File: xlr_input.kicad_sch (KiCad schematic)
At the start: 6 parts, among them J1 XLR3, J2 Conn_02x05_Counter_Clockwise, J2 XLR3, J3 XLR3, J4 XLR3, SW1 SW_SPDT

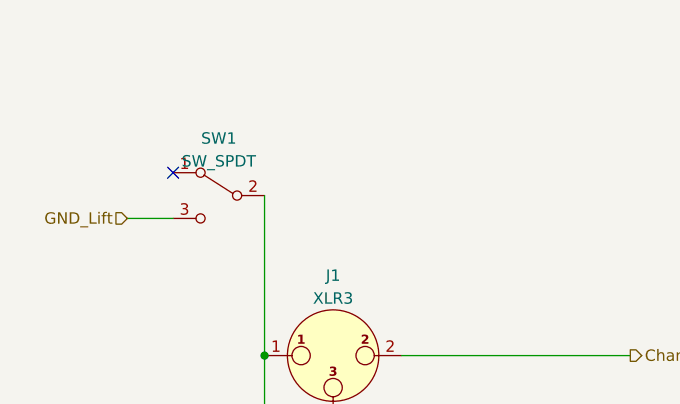
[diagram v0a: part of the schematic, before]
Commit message: Finished up schematic, before board splitting
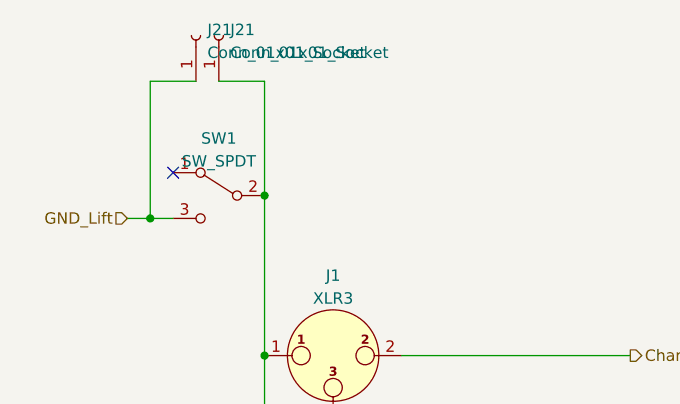
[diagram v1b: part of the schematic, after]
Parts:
- added J21 (x2): Conn_01x01_Socket, Connector_Wire:SolderWire-0.75sqmm_1x01_D1.25mm_OD2.3mm, symbol Connector:Conn_01x01_Socket
- J2: footprint (none) -> Connector_PinSocket_2.54mm:PinSocket_2x05_P2.54mm_Vertical
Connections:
- net GND_Lift: now also J21.1 (Pin_1)
- net at J1.1, J2.1, J3.1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: now also J21.1 (Pin_1)
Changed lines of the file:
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@@
   (junction (at 81.28 93.98) (diameter 0) (color 0 0 0 0)
+  )
+  (junction (at 81.28 57.15) (diameter 0) (color 0 0 0 0)
+  )
+  (junction (at 68.58 59.69) (diameter 0) (color 0 0 0 0)
   )
   (junction (at 81.28 74.93) (diameter 0) (color 0 0 0 0)
@@
     (stroke (width 0) (type default))
   )
+  (wire (pts (xy 68.58 44.45) (xy 73.66 44.45))
+    (stroke (width 0) (type default))
+  )
   (wire (pts (xy 88.9 139.7) (xy 121.92 139.7))
     (stroke (width 0) (type default))
   )
+  (wire (pts (xy 76.2 44.45) (xy 81.28 44.45))
+    (stroke (width 0) (type default))
+  )
   (wire (pts (xy 96.52 93.98) (xy 121.92 93.98))
     (stroke (width 0) (type default))
@@
     (stroke (width 0) (type default))
   )
-  (wire (pts (xy 71.12 59.69) (xy 66.04 59.69))
+  (wire (pts (xy 71.12 59.69) (xy 68.58 59.69))
+    (stroke (width 0) (type default))
+  )
+  (wire (pts (xy 68.58 59.69) (xy 68.58 44.45))
     (stroke (width 0) (type default))
   )
@@
   )
   (wire (pts (xy 81.28 57.15) (xy 81.28 74.93))
+    (stroke (width 0) (type default))
+  )
+  (wire (pts (xy 68.58 59.69) (xy 66.04 59.69))
+    (stroke (width 0) (type default))
+  )
+  (wire (pts (xy 81.28 44.45) (xy 81.28 57.15))
     (stroke (width 0) (type default))
   )
@@
       (effects (font (size 1.27 1.27)))
     )
-    (property "Footprint" "" (at 175.26 94.615 0)
+    (property "Footprint" "Connector_PinSocket_2.54mm:PinSocket_2x05_P2.54mm_Vertical" (at 175.26 94.615 0)
       (effects (font (size 1.27 1.27)) hide)
     )
@@
         )
       )
+    )
+  )
+  (symbol (lib_id "Connector:Conn_01x01_Socket") (at 73.66 39.37 90) (unit 1)
+    (in_bom yes) (on_board yes) (dnp no) (fields_autoplaced)
+    (property "Reference" "J21" (at 74.93 38.735 90)
+      (effects (font (size 1.27 1.27)) (justify right))
+    )
+    (property "Value" "Conn_01x01_Socket" (at 74.93 41.275 90)
+      (effects (font (size 1.27 1.27)) (justify right))
+    )
+    (property "Footprint" "Connector_Wire:SolderWire-0.75sqmm_1x01_D1.25mm_OD2.3mm" (at 73.66 39.37 0)
+      (effects (font (size 1.27 1.27)) hide)
+    )
+    (property "Datasheet" "~" (at 73.66 39.37 0)
+      (effects (font (size 1.27 1.27)) hide)
+    )
+    (pin "1")
+    (instances
+      (project "EF_matrix"
+        (path "/621f65ee-d66d-40b7-9a89-3052b9373190/b97d10d9-dc84-4d90-b1cc-f43ccd4b156b"
+          (reference "J21") (unit 1)
+        )
+        (path "/621f65ee-d66d-40b7-9a89-3052b9373190/837cbbaa-ad41-4de8-bb02-f85faf12da13"
+          (reference "J22") (unit 1)
+        )
+        (path "/621f65ee-d66d-40b7-9a89-3052b9373190/64851fbd-c688-4197-a63d-3dce17468ba2"
+          (reference "J23") (unit 1)
+        )
+      )
+    )
+  )
+  (symbol (lib_id "Connector:Conn_01x01_Socket") (at 76.2 39.37 90) (unit 1)
+    (in_bom yes) (on_board yes) (dnp no) (fields_autoplaced)
+    (property "Reference" "J21" (at 77.47 38.735 90)
+      (effects (font (size 1.27 1.27)) (justify right))
+    )
+    (property "Value" "Conn_01x01_Socket" (at 77.47 41.275 90)
+      (effects (font (size 1.27 1.27)) (justify right))
+    )
+    (property "Footprint" "Connector_Wire:SolderWire-0.75sqmm_1x01_D1.25mm_OD2.3mm" (at 76.2 39.37 0)
+      (effects (font (size 1.27 1.27)) hide)
+    )
+    (property "Datasheet" "~" (at 76.2 39.37 0)
+      (effects (font (size 1.27 1.27)) hide)
+    )
+    (pin "1")
+    (instances
+      (project "EF_matrix"
+        (path "/621f65ee-d66d-40b7-9a89-3052b9373190/b97d10d9-dc84-4d90-b1cc-f43ccd4b156b"
+          (reference "J21") (unit 1)
+        )
+        (path "/621f65ee-d66d-40b7-9a89-3052b9373190/837cbbaa-ad41-4de8-bb02-f85faf12da13"
+          (reference "J25") (unit 1)
+        )
+        (path "/621f65ee-d66d-40b7-9a89-3052b9373190/64851fbd-c688-4197-a63d-3dce17468ba2"
+          (reference "J26") (unit 1)
+        )
+      )

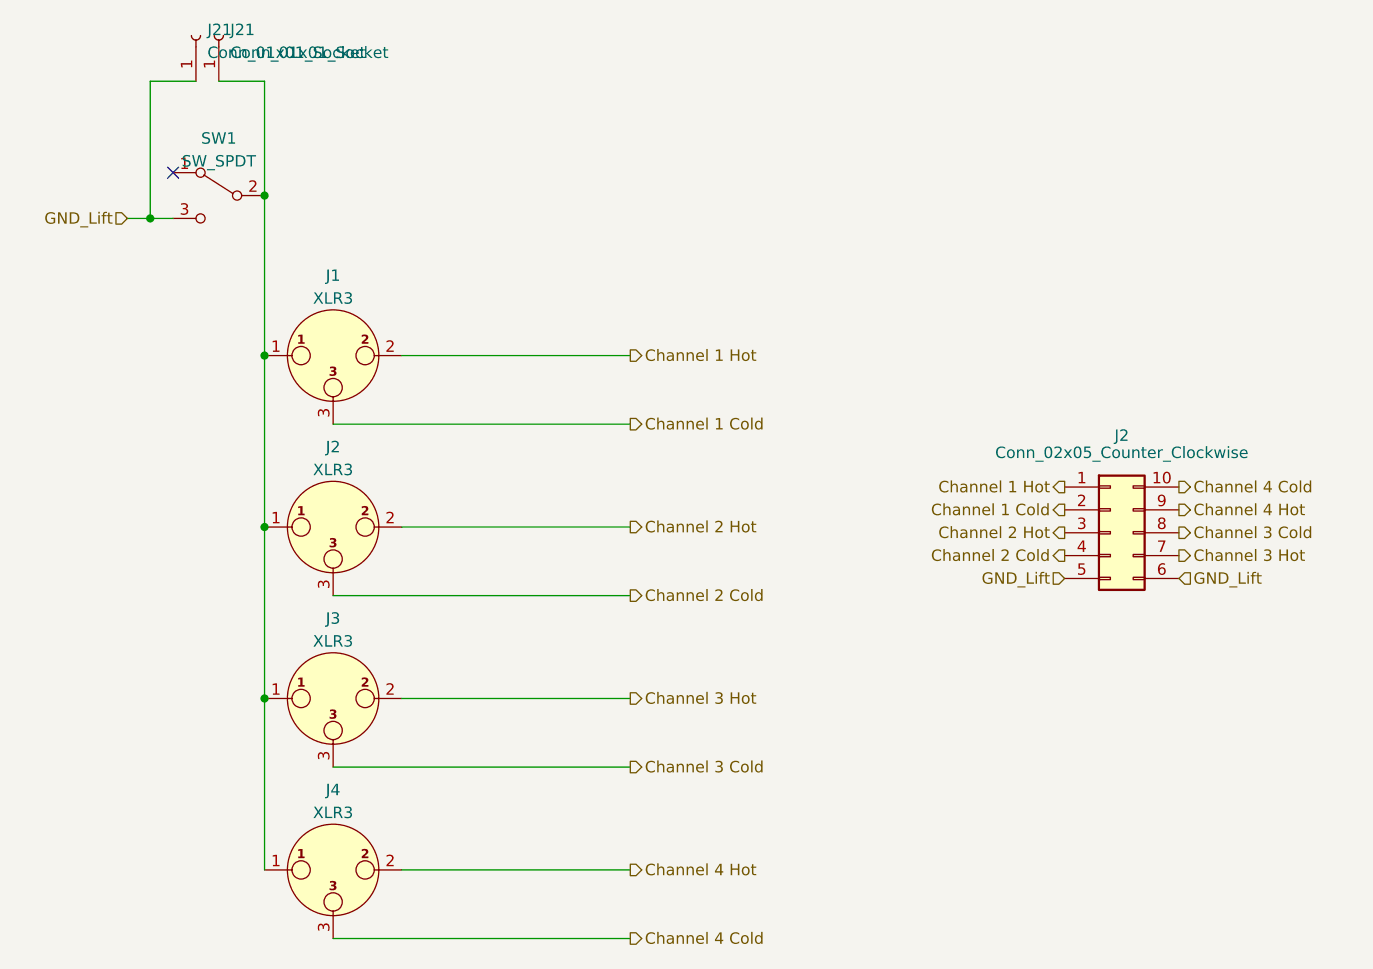
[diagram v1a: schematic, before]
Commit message: Changed position of ribbon connectors, added DC
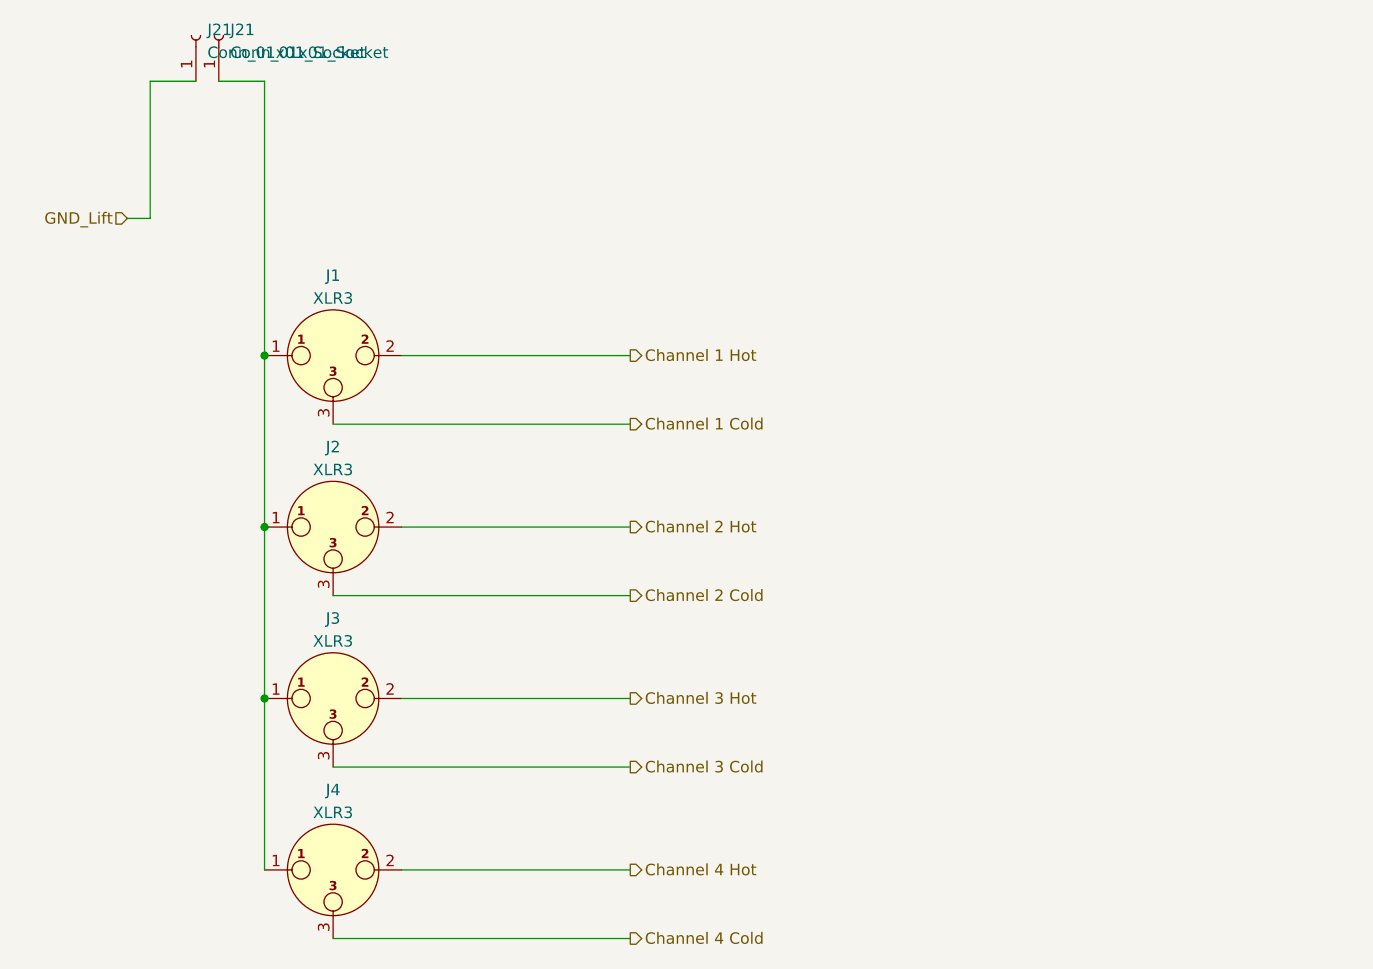
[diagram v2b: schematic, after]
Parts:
- removed J2: Conn_02x05_Counter_Clockwise, Connector_PinSocket_2.54mm:PinSocket_2x05_P2.54mm_Vertical, symbol Connector_Generic:Conn_02x05_Counter_Clockwise
- removed SW1: SW_SPDT, symbol Switch:SW_SPDT
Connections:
- no-connect marks 1 -> 0
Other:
- company: (none) -> Daniel Machnik Sounddesign und Tontechnik
- title: (none) -> Essigfabrik 2-Way PA Switcher
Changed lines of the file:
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@@
 (kicad_sch (version 20230121) (generator eeschema)
   (paper "A4")
+  (title_block
+    (title "Essigfabrik 2-Way PA Switcher")
+    (date "2023-11-21")
+    (rev "1")
+    (company "Daniel Machnik Sounddesign und Tontechnik")
+  )
   (junction (at 81.28 113.03) (diameter 0) (color 0 0 0 0)
   )
   (junction (at 81.28 93.98) (diameter 0) (color 0 0 0 0)
   )
-  (junction (at 81.28 57.15) (diameter 0) (color 0 0 0 0)
-  )
-  (junction (at 68.58 59.69) (diameter 0) (color 0 0 0 0)
-  )
   (junction (at 81.28 74.93) (diameter 0) (color 0 0 0 0)
   )
-  (no_connect (at 71.12 54.61))
   (wire (pts (xy 81.28 74.93) (xy 81.28 93.98))
     (stroke (width 0) (type default))
@@
     (stroke (width 0) (type default))
   )
-  (wire (pts (xy 71.12 59.69) (xy 68.58 59.69))
-    (stroke (width 0) (type default))
-  )
   (wire (pts (xy 68.58 59.69) (xy 68.58 44.45))
     (stroke (width 0) (type default))
@@
     (stroke (width 0) (type default))
   )
-  (wire (pts (xy 81.28 57.15) (xy 81.28 74.93))
+  (wire (pts (xy 81.28 44.45) (xy 81.28 74.93))
     (stroke (width 0) (type default))
   )
@@
     (stroke (width 0) (type default))
   )
-  (wire (pts (xy 81.28 44.45) (xy 81.28 57.15))
-    (stroke (width 0) (type default))
-  )
-  (hierarchical_label "Channel 4 Hot" (shape output) (at 182.88 92.075 0) (fields_autoplaced)
-    (effects (font (size 1.27 1.27)) (justify left))
-  )
   (hierarchical_label "Channel 1 Cold" (shape output) (at 121.92 82.55 0) (fields_autoplaced)
-    (effects (font (size 1.27 1.27)) (justify left))
-  )
-  (hierarchical_label "Channel 4 Cold" (shape output) (at 182.88 89.535 0) (fields_autoplaced)
     (effects (font (size 1.27 1.27)) (justify left))
   )
@@
     (effects (font (size 1.27 1.27)) (justify right))
   )
-  (hierarchical_label "Channel 3 Hot" (shape output) (at 182.88 97.155 0) (fields_autoplaced)
-    (effects (font (size 1.27 1.27)) (justify left))
-  )
-  (hierarchical_label "Channel 1 Hot" (shape output) (at 170.18 89.535 180) (fields_autoplaced)
-    (effects (font (size 1.27 1.27)) (justify right))
-  )
-  (hierarchical_label "Channel 3 Cold" (shape output) (at 182.88 94.615 0) (fields_autoplaced)
-    (effects (font (size 1.27 1.27)) (justify left))
-  )
   (hierarchical_label "Channel 1 Hot" (shape output) (at 121.92 74.93 0) (fields_autoplaced)
     (effects (font (size 1.27 1.27)) (justify left))
   )
-  (hierarchical_label "GND_Lift" (shape input) (at 170.18 99.695 180) (fields_autoplaced)
-    (effects (font (size 1.27 1.27)) (justify right))
-  )
-  (hierarchical_label "Channel 1 Cold" (shape output) (at 170.18 92.075 180) (fields_autoplaced)
-    (effects (font (size 1.27 1.27)) (justify right))
-  )
   (hierarchical_label "Channel 2 Hot" (shape output) (at 121.92 93.98 0) (fields_autoplaced)
     (effects (font (size 1.27 1.27)) (justify left))
-  )
-  (hierarchical_label "Channel 2 Hot" (shape output) (at 170.18 94.615 180) (fields_autoplaced)
-    (effects (font (size 1.27 1.27)) (justify right))
   )
   (hierarchical_label "Channel 3 Hot" (shape output) (at 121.92 113.03 0) (fields_autoplaced)
@@
     (effects (font (size 1.27 1.27)) (justify left))
   )
-  (hierarchical_label "Channel 2 Cold" (shape output) (at 170.18 97.155 180) (fields_autoplaced)
-    (effects (font (size 1.27 1.27)) (justify right))
-  )
   (hierarchical_label "Channel 4 Cold" (shape output) (at 121.92 139.7 0) (fields_autoplaced)
     (effects (font (size 1.27 1.27)) (justify left))
   )
   (hierarchical_label "Channel 3 Cold" (shape output) (at 121.92 120.65 0) (fields_autoplaced)
-    (effects (font (size 1.27 1.27)) (justify left))
-  )
-  (hierarchical_label "GND_Lift" (shape input) (at 182.88 99.695 0) (fields_autoplaced)
     (effects (font (size 1.27 1.27)) (justify left))
   )
@@
     )
   )
-  (symbol (lib_id "Connector_Generic:Conn_02x05_Counter_Clockwise") (at 175.26 94.615 0) (unit 1)
-    (in_bom yes) (on_board yes) (dnp no)
-    (property "Reference" "J2" (at 176.53 83.82 0)
-      (effects (font (size 1.27 1.27)))
-    )
-    (property "Value" "Conn_02x05_Counter_Clockwise" (at 176.53 85.725 0)
-      (effects (font (size 1.27 1.27)))
-    )
-    (property "Footprint" "Connector_PinSocket_2.54mm:PinSocket_2x05_P2.54mm_Vertical" (at 175.26 94.615 0)
-      (effects (font (size 1.27 1.27)) hide)
-    )
-    (property "Datasheet" "~" (at 175.26 94.615 0)
-      (effects (font (size 1.27 1.27)) hide)
-    )
-    (pin "1")
-    (pin "10")
-    (pin "2")
-    (pin "3")
-    (pin "4")
-    (pin "5")
-    (pin "6")
-    (pin "7")
-    (pin "8")
-    (pin "9")
-    (instances
-      (project "EF_matrix"
-        (path "/621f65ee-d66d-40b7-9a89-3052b9373190/d94772af-2feb-48c7-98be-bb0e397012c8"
-          (reference "J2") (unit 1)
-        )
-        (path "/621f65ee-d66d-40b7-9a89-3052b9373190/837cbbaa-ad41-4de8-bb02-f85faf12da13"
-          (reference "J1") (unit 1)
-        )
-        (path "/621f65ee-d66d-40b7-9a89-3052b9373190/64851fbd-c688-4197-a63d-3dce17468ba2"
-          (reference "J3") (unit 1)
-        )
-      )
-    )
-  )
   (symbol (lib_id "Connector_Audio:XLR3") (at 88.9 74.93 0) (unit 1)
     (in_bom yes) (on_board yes) (dnp no) (fields_autoplaced)
@@
         )
       )
-    )
-  )
-  (symbol (lib_id "Switch:SW_SPDT") (at 76.2 57.15 0) (mirror y) (unit 1)
-    (in_bom yes) (on_board yes) (dnp no)
-    (property "Reference" "SW1" (at 76.2 50.8 0)
-      (effects (font (size 1.27 1.27)))
-    )
-    (property "Value" "SW_SPDT" (at 76.2 53.34 0)
-      (effects (font (size 1.27 1.27)))
-    )
-    (property "Footprint" "" (at 76.2 57.15 0)
-      (effects (font (size 1.27 1.27)) hide)
-    )
-    (property "Datasheet" "~" (at 76.2 57.15 0)
-      (effects (font (size 1.27 1.27)) hide)
-    )
-    (pin "1")
-    (pin "2")
-    (pin "3")
-    (instances
-      (project "EF_matrix"
-        (path "/621f65ee-d66d-40b7-9a89-3052b9373190"
-          (reference "SW1") (unit 1)
-        )
-        (path "/621f65ee-d66d-40b7-9a89-3052b9373190/837cbbaa-ad41-4de8-bb02-f85faf12da13"
-          (reference "SW2") (unit 1)
-        )
-        (path "/621f65ee-d66d-40b7-9a89-3052b9373190/64851fbd-c688-4197-a63d-3dce17468ba2"
-          (reference "SW3") (unit 1)
-        )
-      )
